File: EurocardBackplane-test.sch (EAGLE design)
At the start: 9 parts, among them IC1 LM399H, U1 MIC5209, U2 MIC5209, X1 FAC64S, X2 FAC64S

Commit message: Mostly-routed test board with teensy, WIZNET, and vref.
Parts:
- removed U2: MIC5209, regulator-jqi:MIC5209
- removed X1, X2: FAC64S, Eurocard-Backplane-jqi:FAC64S
- added C1, C4, C5, C6: 1uF, jqi_passives:C_MLCC_SMDCMLCC_0603
- added J1: JUMPER, Eurocard-Backplane-jqi:JUMPER
- added R3, R4: (no value), jqi_passives:R_SMDR0603
- added R5: 7.5k, jqi_passives:R_SMDR0603
- added U3: MIC5209-3.3YS, regulator-jqi:MIC5209-FIXED
- added X5, X6, X7_AUX: FAC64S, Eurocard-Backplane-jqi:FAC64S
- renumbered U$4 to TEENSY
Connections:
- removed net HV_INTERLOCK1: X2.A25, X2.C25
- removed net I2C_SCL1: X2.C14
- removed net I2C_SDA1: X2.A14
- removed net N$2: X2.C11
- removed net N$23: X1.A30, X1.C30
- removed net N$24: X1.A32, X1.C32
- removed net N$25: X1.A26, X1.C26
- removed net N$26: X1.A27, X1.C27
- removed net N$3: X2.A10
- removed net SPI_CS: X1.C12
- removed net SPI_CS1: X2.C12
- removed net SPI_MISO1: X2.C13
- removed net SPI_MOSI1: X2.A13
- removed net SPI_SCLK1: X2.A12
- new net -15V: X3-1.S, X5.A30, X5.C30, X6.A30, X6.C30, X7_AUX.A30, X7_AUX.C30
- new net A15: X5.A15, X6.A15, X7_AUX.A15
- new net A16: X5.A16, X6.A16, X7_AUX.A16
- new net A17: X5.A17, X6.A17, X7_AUX.A17
- new net A18: X5.A18, X6.A18, X7_AUX.A18
- new net A19: X5.A19, X6.A19, X7_AUX.A19
- new net A2: X5.A2, X6.A2, X7_AUX.A2
- new net A20: X5.A20, X6.A20, X7_AUX.A20
- new net A21: X5.A21, X6.A21, X7_AUX.A21
- new net A22: X5.A22, X6.A22, X7_AUX.A22
- new net A23: X5.A23, X6.A23, X7_AUX.A23
- new net A27: X5.A27, X6.A27, X7_AUX.A27
- new net A28: X5.A28, X6.A28, X7_AUX.A28
- new net A29: X5.A29, X6.A29, X7_AUX.A29
- new net A5: X5.A5, X6.A5, X7_AUX.A5
- new net A8: X5.A8, X6.A8, X7_AUX.A8
- new net A9: X5.A9, X6.A9, X7_AUX.A9
- new net C15: X5.C15, X6.C15, X7_AUX.C15
- new net C16: X5.C16, X6.C16, X7_AUX.C16
- new net C17: X5.C17, X6.C17, X7_AUX.C17
- new net C18: X5.C18, X6.C18, X7_AUX.C18
- new net C19: X5.C19, X6.C19, X7_AUX.C19
- new net C2: X5.C2, X6.C2, X7_AUX.C2
- new net C20: X5.C20, X6.C20, X7_AUX.C20
- new net C21: X5.C21, X6.C21, X7_AUX.C21
- new net C22: X5.C22, X6.C22, X7_AUX.C22
- new net C23: X5.C23, X6.C23, X7_AUX.C23
- new net C27: X5.C27, X6.C27, X7_AUX.C27
- new net C28: X5.C28, X6.C28, X7_AUX.C28
- new net C29: X5.C29, X6.C29, X7_AUX.C29
- new net C5: X5.C5, X6.C5, X7_AUX.C5
- new net C8: X5.C8, X6.C8, X7_AUX.C8
- new net C9: X5.C9, X6.C9, X7_AUX.C9
- new net HV: X5.A26, X5.C26, X6.A26, X6.C26, X7_AUX.A26, X7_AUX.C26
- new net N$10: TEENSY.32/T/PWM
- new net N$11: TEENSY.31/A20
- new net N$9: TEENSY.30/A19/SDA1
- new net SPI_CS5: TEENSY.25/T/PWM, X5.C12
- new net SPI_CS6: TEENSY.24, X6.C12
- new net SPI_CS7_AUX: TEENSY.33/T, X7_AUX.C12
- new net VREF: IC1.1, R5.1, X5.A32, X5.C32, X6.A32, X6.C32, X7_AUX.A32, X7_AUX.C32
- net +15V: now also C4.2, IC1.3, R5.2, U1.EN, U1.IN, X3-2.S, X5.A31, X5.C31, X6.A31, X6.C31, X7_AUX.A31, X7_AUX.C31; no longer U2.EN, U2.IN, X1.A31, X1.C31, X2.A31, X2.C31
- net +3V3: now also C5.2, U3.OUT; no longer TEENSY.3.3V
- net D0: now also X5.A10, X6.A10, X7_AUX.A10; no longer X1.A10
- net D1: now also X5.C10, X6.C10, X7_AUX.C10; no longer X1.C10
- net D2: now also X5.A11, X6.A11, X7_AUX.A11; no longer X1.A11
- net D3: now also X5.C11, X6.C11, X7_AUX.C11; no longer X1.C11
- net GND: now also IC1.2, IC1.4, J1.P$2, TEENSY.AGND, X3-3.S, X3-4.S, X5.A1, X5.A25, X5.C1, X5.C25, X6.A1, X6.A25, X6.C1, X6.C25, X7_AUX.A1, X7_AUX.A25, X7_AUX.C1, X7_AUX.C25; no longer X1.A1, X1.C1, X2.A1, X2.C1
- net GPIO#1: now also TEENSY.22/A8/T/PWM; no longer TEENSY.14/A0
- net GPIO#2: now also TEENSY.21/A7/PWM; no longer TEENSY.15/A1/T
- net GPIO#3: now also TEENSY.20/A6/PWM; no longer TEENSY.16/A2/T
- net GPIO#5: now also TEENSY.16/A2/T; no longer TEENSY.20/A6/PWM
- net GPIO#6: now also TEENSY.15/A1/T; no longer TEENSY.21/A7/PWM
- net GPIO#7: now also TEENSY.14/A0; no longer TEENSY.22/A8/T/PWM
- net GPIO0: now also X5.A3, X6.A3, X7_AUX.A3; no longer X1.A3, X2.A3
- net GPIO1: now also X5.C3, X6.C3, X7_AUX.C3; no longer X1.C3, X2.C3
- net GPIO2: now also X5.A4, X6.A4, X7_AUX.A4; no longer X1.A4, X2.A4
- net GPIO3: now also X5.C4, X6.C4, X7_AUX.C4; no longer X1.C4, X2.C4
- net GPIO4: now also X5.A6, X6.A6, X7_AUX.A6; no longer X1.A6, X2.A6
- net GPIO5: now also X5.C6, X6.C6, X7_AUX.C6; no longer X1.C6, X2.C6
- net GPIO6: now also X5.A7, X6.A7, X7_AUX.A7; no longer X1.A7, X2.A7
- net GPIO7: now also X5.C7, X6.C7, X7_AUX.C7; no longer X1.C7, X2.C7
- net HV_INTERLOCK: now also X5.A24, X5.C24, X6.A24, X6.C24, X7_AUX.A24, X7_AUX.C24; no longer X1.A25, X1.C25
- net I2C_SCL: now also X5.C14, X6.C14, X7_AUX.C14; no longer X1.C14
- net I2C_SDA: now also X5.A14, X6.A14, X7_AUX.A14; no longer X1.A14
- net N$1: now also TEENSY.23/A9/T/PWM; no longer X2.C10
- net N$4: now also TEENSY.26/A15; no longer X2.A11
- net N$5: now also R3.1, R4.2, U1.FB; no longer X2.A30, X2.C30
- net N$6: now also TEENSY.27/A16; no longer X2.A32, X2.C32
- net N$7: now also TEENSY.28/A17; no longer X2.A26, X2.C26
- net N$8: now also TEENSY.29/A18/SCL1; no longer X2.A27, X2.C27
- net SPI_MISO: now also X5.C13, X6.C13, X7_AUX.C13; no longer X1.C13
- net SPI_MOSI: now also X5.A13, X6.A13, X7_AUX.A13; no longer X1.A13
- net SPI_SCLK: now also X5.A12, X6.A12, X7_AUX.A12; no longer X1.A12
- net VDD: now also C1.2, C6.2, R3.2, U1.OUT, U3.IN
- net VSS: now also C1.1, C4.1, C5.1, C6.1, J1.P$1, R4.1, U1.GND, U3.GND
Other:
- note added: "+5V"
- note added: "JQI LOGO!!!"
- note removed: "MISO"
- note removed: "MOSI"

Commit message: routing and layout of test board done
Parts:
- added C2, C3: (no value), jqi_passives:C_POL_SMDF
- added D1: (no value), diode:DIODE-SOD523
- added L1: (no value), jqi_passives:L_FERRITE_SMDLFERRITE_0805
- renumbered U$2 to U2
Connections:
- net N$11 renamed SPI_CS4
- net N$6 renamed SPI_C0
- net N$7 renamed SPI_CS1
- net N$8 renamed SPI_CS2
- net N$9 renamed SPI_CS3
- removed net N$10: TEENSY.32/T/PWM
- removed net N$4: TEENSY.26/A15
- new net N$2: D1.A, TEENSY.VUSB
- net +15V: now also C2.+, L1.1; no longer C4.2, U1.EN, U1.IN
- net -15V: now also C3.-
- net D0: now also TEENSY.0/RX1/T; no longer TEENSY.4/CAN-RX-PWM
- net D3: now also TEENSY.4/CAN-RX-PWM; no longer TEENSY.0/RX1/T
- net GND: now also C2.-, C3.+
- net N$1: now also C4.2, L1.2, U1.EN, U1.IN; no longer TEENSY.23/A9/T/PWM
- net SPI_CS5: now also TEENSY.32/T/PWM; no longer TEENSY.25/T/PWM
- net SPI_CS6: now also TEENSY.33/T; no longer TEENSY.24
- net SPI_CS7_AUX: now also TEENSY.25/T/PWM; no longer TEENSY.33/T
- net VDD: now also D1.C
- net WIZNET_INTERRUPT: now also TEENSY.10/TX2/PWM; no longer TEENSY.8/TX3
- net WIZNET_PWDN: now also TEENSY.7/RX3; no longer TEENSY.9/RX2/PWM
- net WIZNET_RESET: now also TEENSY.9/RX2/PWM; no longer TEENSY.7/RX3
- net WIZNET_SS: now also TEENSY.8/TX3; no longer TEENSY.10/TX2/PWM
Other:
- note added: "568-7397-1-ND"

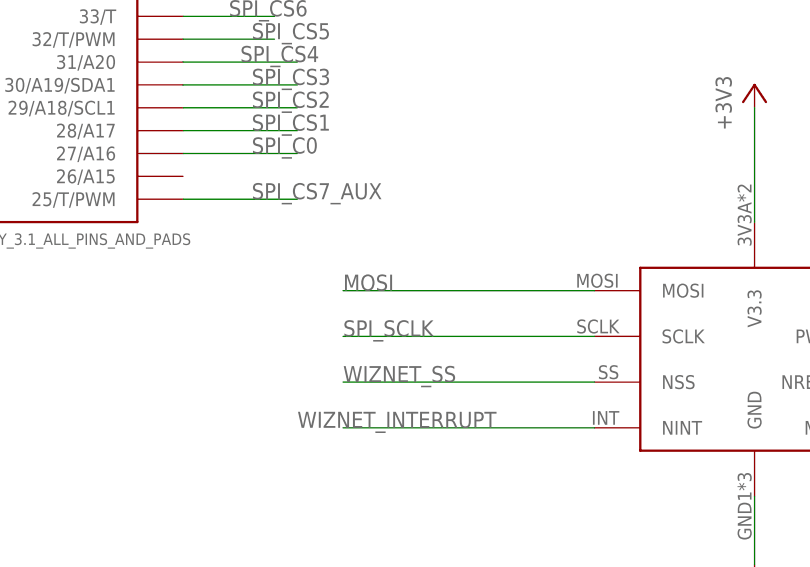
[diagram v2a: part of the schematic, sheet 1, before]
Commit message: updated test backplane
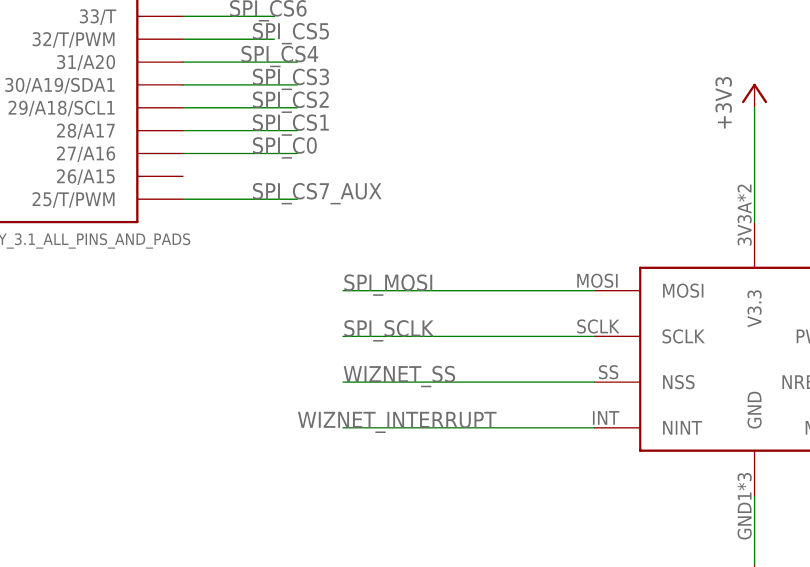
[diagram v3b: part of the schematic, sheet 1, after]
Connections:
- removed net MOSI: U2.MOSI
- net SPI_MOSI: now also U2.MOSI
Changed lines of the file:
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@@
 <?xml version="1.0" encoding="utf-8"?>
 <!DOCTYPE eagle SYSTEM "eagle.dtd">
-<eagle version="6.5.0">
+<eagle version="6.6.0">
 <drawing>
 <settings>
@@
 <setting verticaltext="up"/>
 </settings>
-<grid distance="0.05" unitdist="inch" unit="inch" style="lines" multiple="1" display="no" altdistance="0.01" altunitdist="inch" altunit="inch"/>
+<grid distance="0.1" unitdist="inch" unit="inch" style="lines" multiple="1" display="no" altdistance="0.01" altunitdist="inch" altunit="inch"/>
 <layers>
 <layer number="1" name="Top" color="4" fill="1" visible="no" active="no"/>
@@
 </segment>
 </net>
-<net name="MOSI" class="0">
-<segment>
-<pinref part="U2" gate="G$1" pin="MOSI"/>
-<wire x1="241.3" y1="10.16" x2="213.36" y2="10.16" width="0.1524" layer="91"/>
-<label x="213.36" y="10.16" size="1.778" layer="95"/>
-</segment>
-</net>
 <net name="SPI_MISO" class="0">
 <segment>
@@
 <pinref part="TEENSY" gate="G$1" pin="11/MOSI"/>
 </segment>
-</net>
+<segment>
+<pinref part="U2" gate="G$1" pin="MOSI"/>
+<wire x1="241.3" y1="10.16" x2="213.36" y2="10.16" width="0.1524" layer="91"/>
+<label x="213.36" y="10.16" size="1.778" layer="95"/>
+</segment>
+</net>
